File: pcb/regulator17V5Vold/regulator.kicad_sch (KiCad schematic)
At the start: 7 parts, among them J1 Conn_01x05_Socket, J1 WAGO 2061-602, J2 har-flexicon 2,54 MSH-4, J4 Kyocera-009176002001906, U2 ISL3280ExHZ

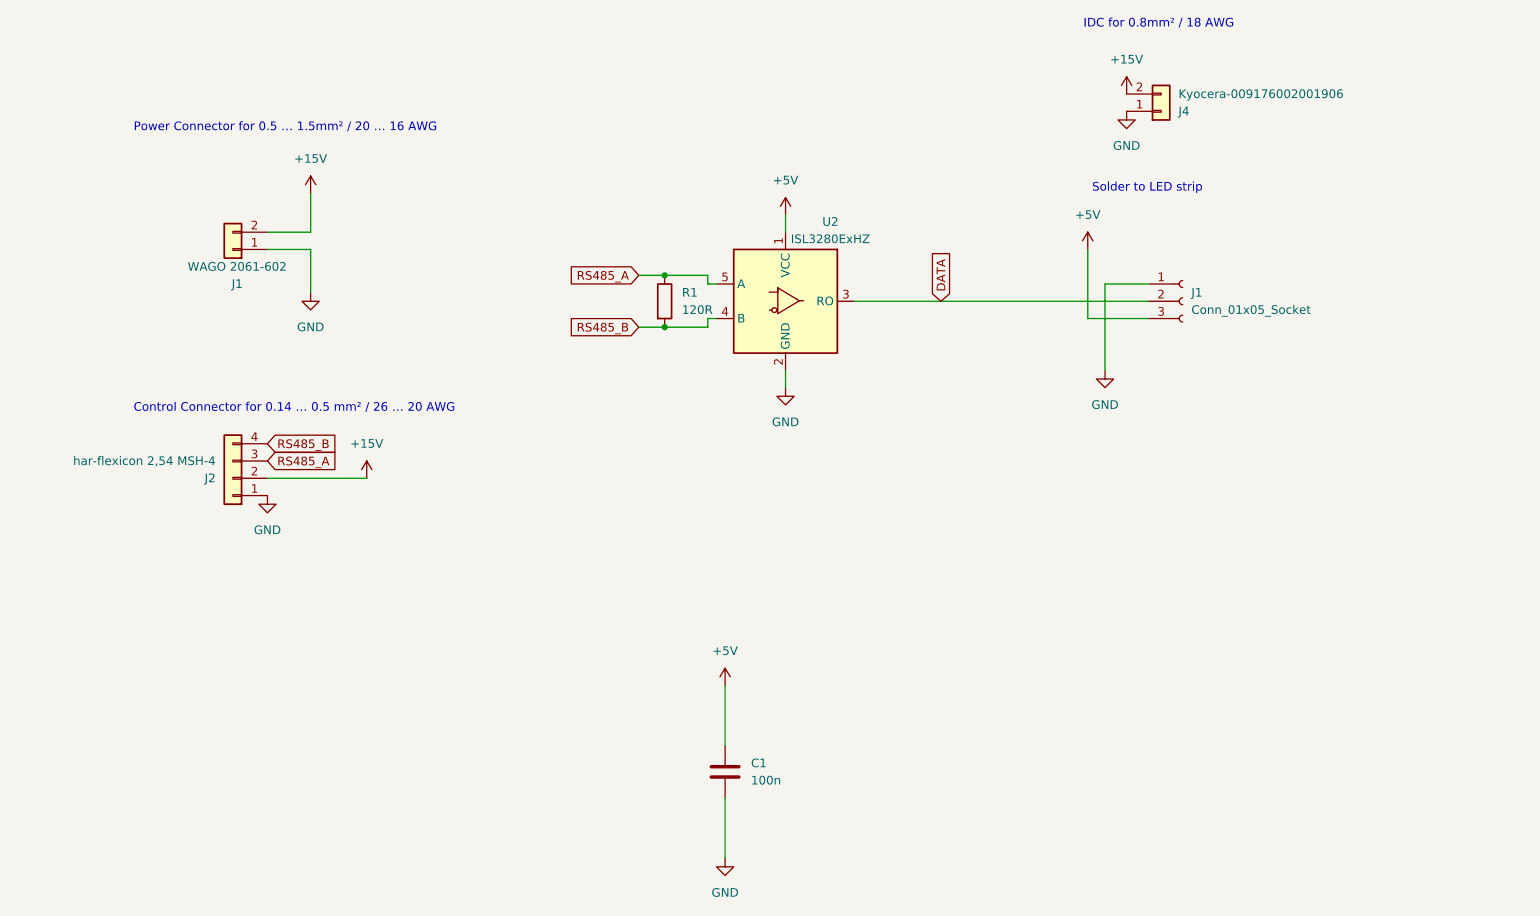
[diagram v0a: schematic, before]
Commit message: Add receiver for IKEA Metod cupboard
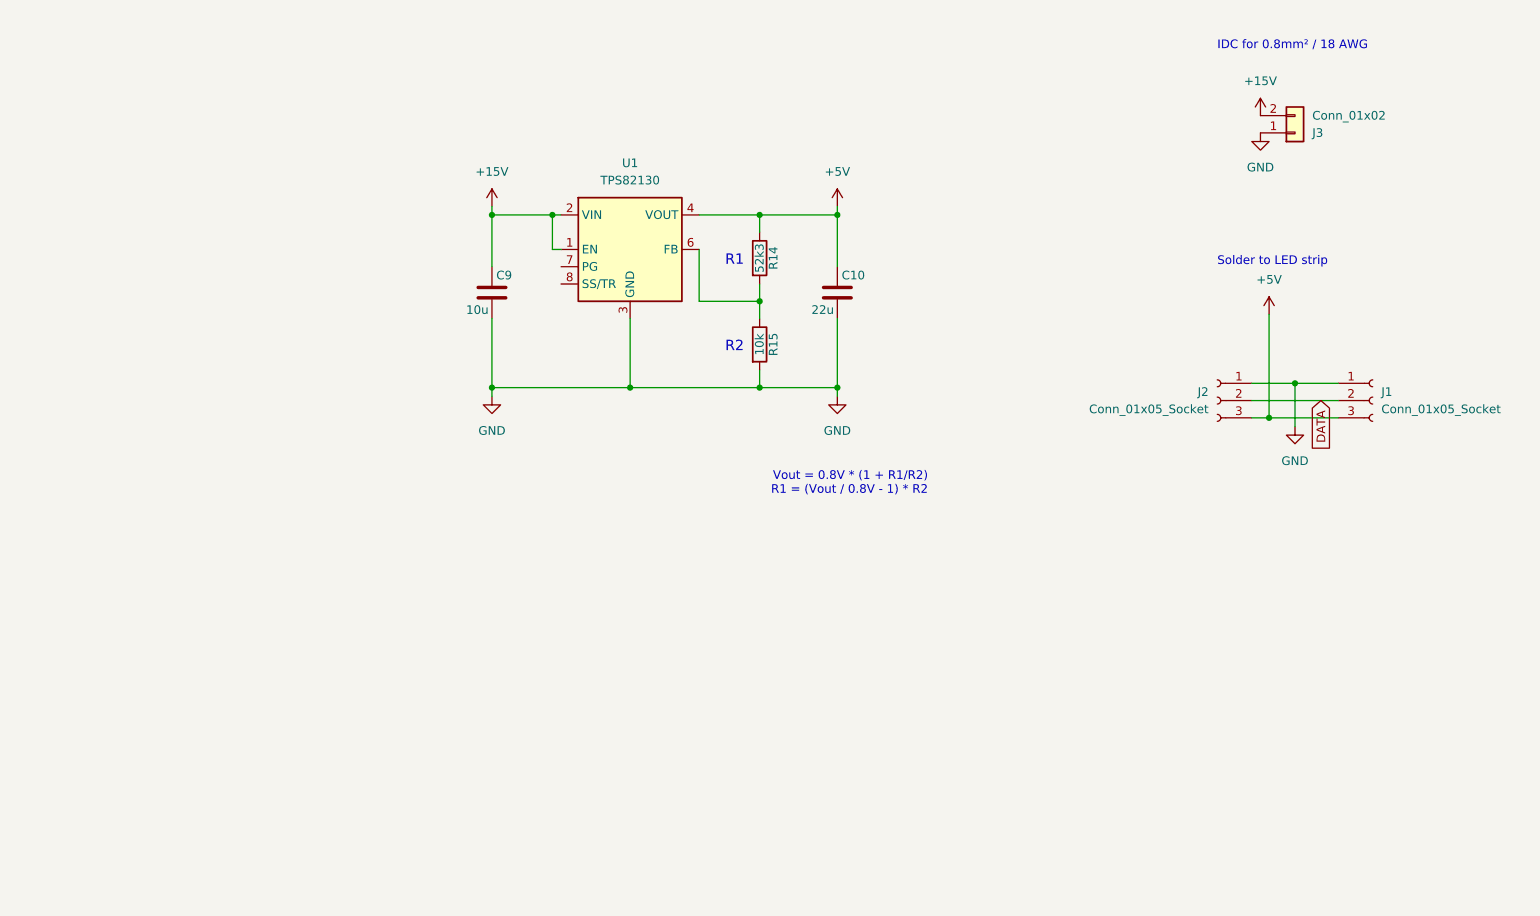
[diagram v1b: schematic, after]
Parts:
- removed C1: 100n, Capacitor_SMD:C_0603_1608Metric, symbol Device:C
- removed J1: WAGO 2061-602, local:WAGO2061-602, symbol Connector_Generic:Conn_01x02
- removed J2: har-flexicon 2,54 MSH-4, local:Harting14110413002000, symbol Connector_Generic:Conn_01x04
- removed J4: Kyocera-009176002001906, local:Kyocera-009176002001906, symbol Connector_Generic:Conn_01x02
- removed R1: 120R, Resistor_SMD:R_1206_3216Metric, symbol Device:R
- removed U2: ISL3280ExHZ, local:ISL3280E, symbol Interface_UART:ISL3280ExHZ
- added C10: 22u, Capacitor_SMD:C_0805_2012Metric, symbol Device:C
- added C9: 10u, Capacitor_SMD:C_1206_3216Metric, symbol Device:C
- added J2: Conn_01x05_Socket, local:Holes, symbol Connector:Conn_01x03_Socket
- added J3: Conn_01x02, local:Kyocera-009176002001906, symbol Connector_Generic:Conn_01x02
- added R14: 52k3, Resistor_SMD:R_0603_1608Metric, symbol Device:R
- added R15: 10k, Resistor_SMD:R_0603_1608Metric, symbol Device:R
- added U1: TPS82130, local:TPS82130, symbol Regulator_Switching:TPS82130
- J1: footprint local:SolderHoles3pin10mm -> local:Holes
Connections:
- net +15V: now also C9.1, J3.2 (Pin_2), U1.1 (EN), U1.2 (VIN)
- net +5V: now also C10.1, J2.3 (Pin_3), R14.1, U1.4 (VOUT), U1.5 (VOUT)
- net DATA: now also J2.2 (Pin_2)
- net GND: now also C10.2, C9.2, J2.1 (Pin_1), J3.1 (Pin_1), R15.2, U1.3 (GND), U1.9 (GND)
- new net: R14.2, R15.1, U1.6 (FB)
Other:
- note added: "R1"
- note added: "R2"
- note added: "Vout = 0.8V * (1 + R1/R2) R1 = (Vout / 0.8V - 1) * R2"
- note removed: "Control Connector for 0.14 … 0.5 mm² / 26 … 20 AWG"
- note removed: "Power Connector for 0.5 … 1.5mm² / 20 … 16 AWG"

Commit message: Use ISL3280E
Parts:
- C10: footprint Capacitor_SMD:C_0805_2012Metric -> local:0805
- C9: footprint Capacitor_SMD:C_1206_3216Metric -> local:1206
- R14, R15: footprint Resistor_SMD:R_0603_1608Metric -> local:0603
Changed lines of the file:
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@@
 			)
 		)
-		(property "Footprint" "Capacitor_SMD:C_0805_2012Metric"
+		(property "Footprint" "local:0805"
 			(at 131.7752 95.25 0)
 			(effects
@@
 			)
 		)
-		(property "Footprint" "Resistor_SMD:R_0603_1608Metric"
+		(property "Footprint" "local:0603"
 			(at 117.602 86.36 90)
 			(effects
@@
 			)
 		)
-		(property "Footprint" "Resistor_SMD:R_0603_1608Metric"
+		(property "Footprint" "local:0603"
 			(at 117.602 99.06 90)
 			(effects
@@
 			)
 		)
-		(property "Footprint" "Capacitor_SMD:C_1206_3216Metric"
+		(property "Footprint" "local:1206"
 			(at 80.9752 95.25 0)
 			(effects
